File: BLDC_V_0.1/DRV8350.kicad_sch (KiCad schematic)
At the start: 12 parts, among them U1 DRV8350SRTVT

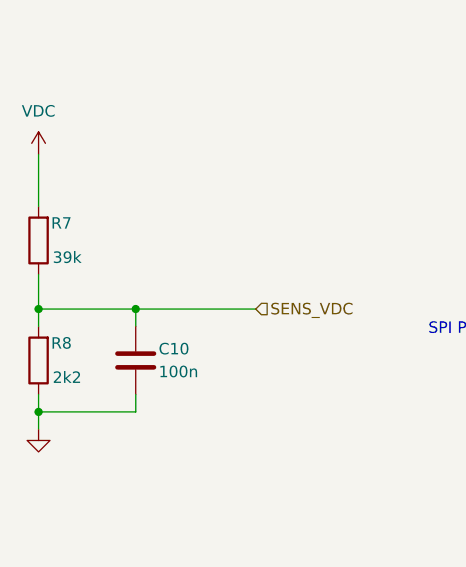
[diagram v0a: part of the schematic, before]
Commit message: Xtal changed 16MHz to 24MHz.
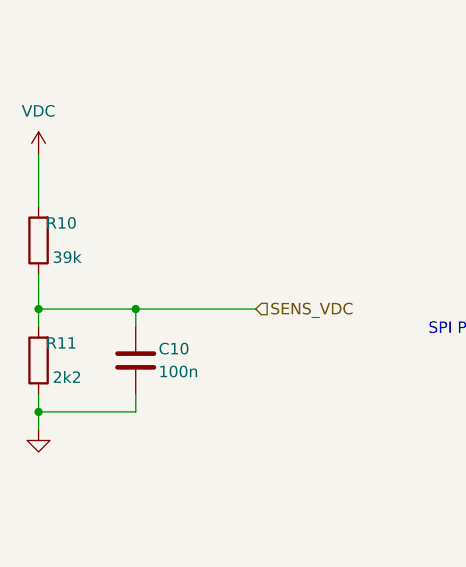
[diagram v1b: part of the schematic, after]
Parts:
- renumbered R7 to R10, R8 to R11
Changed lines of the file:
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@@
   (symbol (lib_id "Device:R") (at 28.575 80.645 180) (unit 1)
     (in_bom yes) (on_board yes) (dnp no)
-    (property "Reference" "R7" (at 31.115 78.74 0)
+    (property "Reference" "R10" (at 31.115 78.74 0)
       (effects (font (size 1.27 1.27)))
     )
@@
   (symbol (lib_id "Device:R") (at 28.575 93.98 180) (unit 1)
     (in_bom yes) (on_board yes) (dnp no)
-    (property "Reference" "R8" (at 31.115 92.075 0)
-      (effects (font (size 1.27 1.27)))
-    )
+    (property "Reference" "R11" (at 31.115 92.075 0)
+      (effects (font (size 1.27 1.27)))
+    )

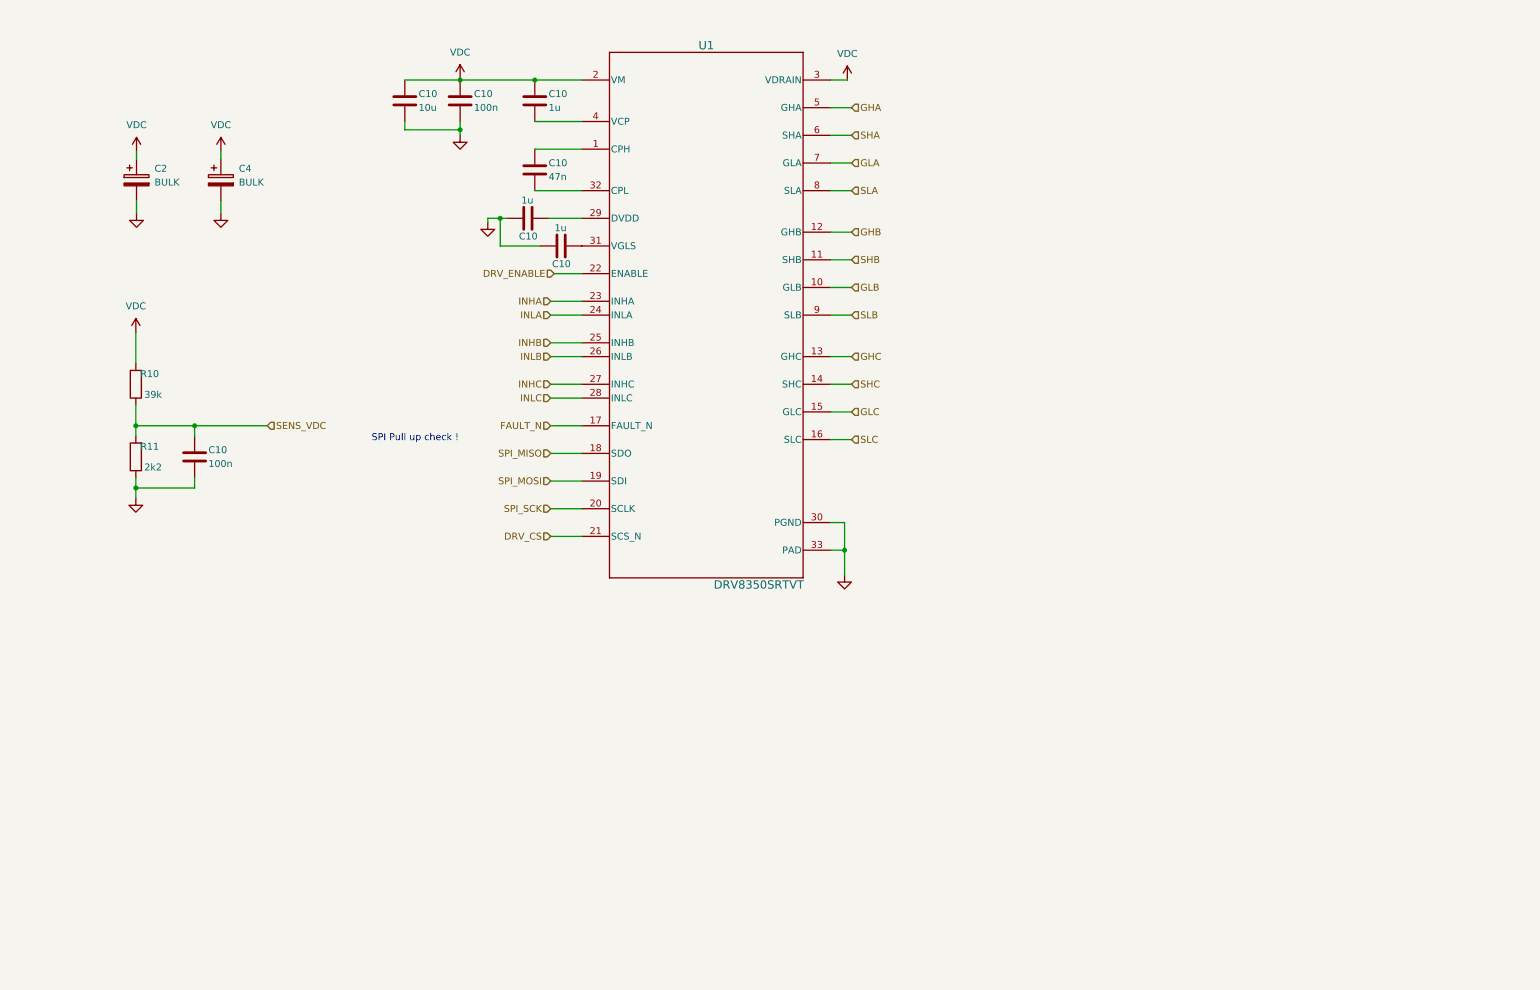
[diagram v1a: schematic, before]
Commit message: Connectors and CAN circuit added.
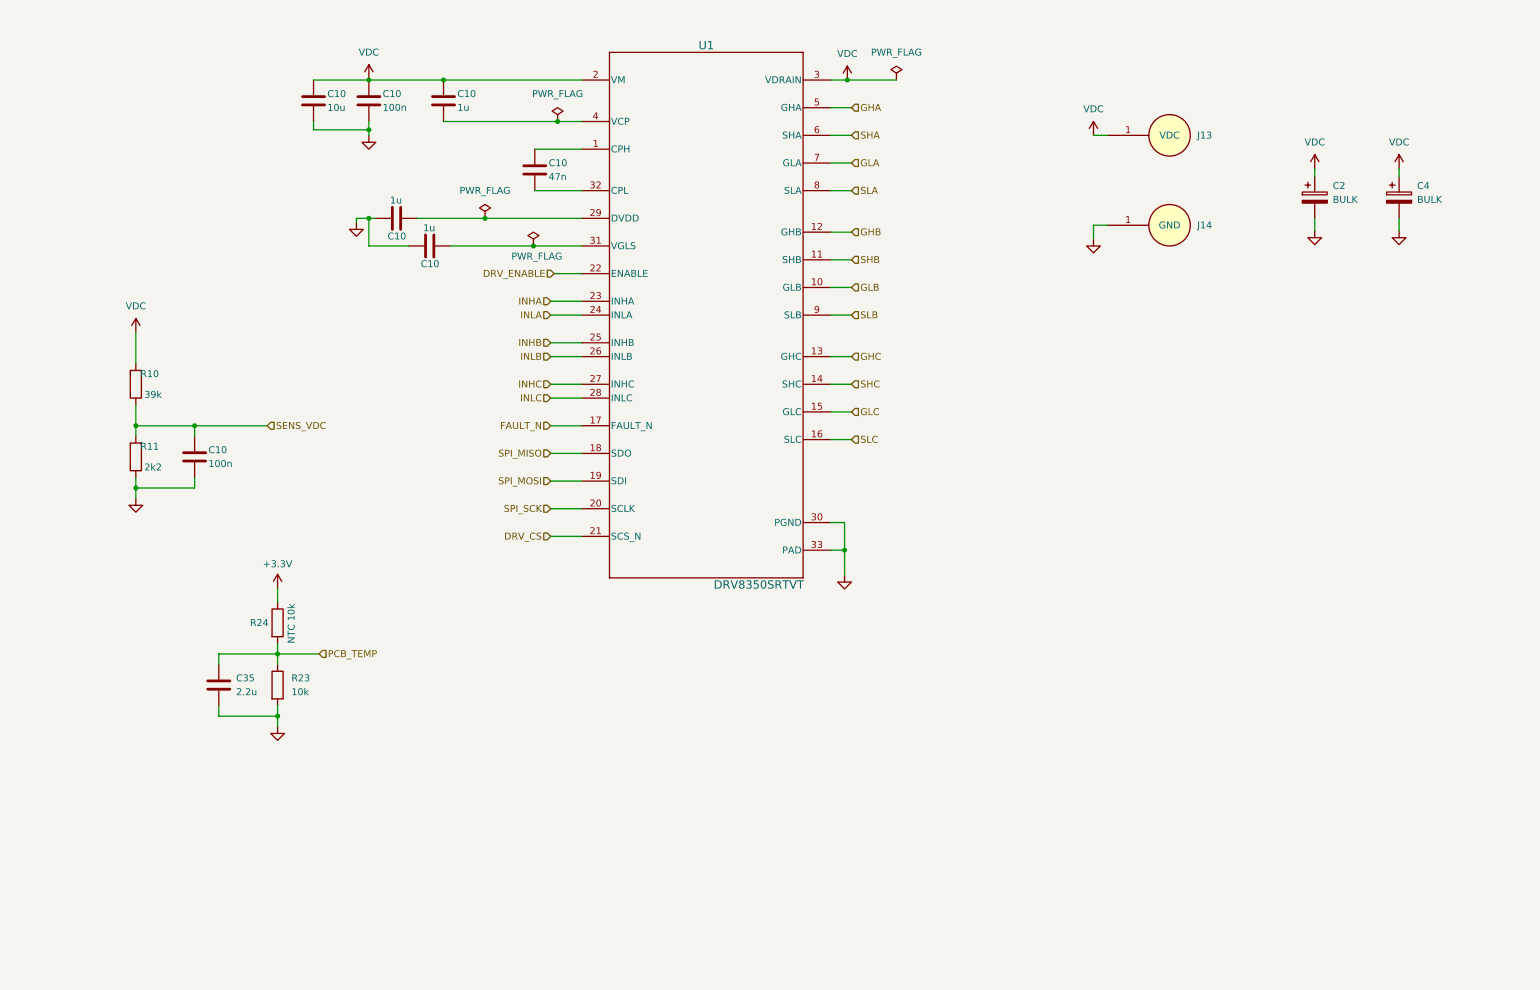
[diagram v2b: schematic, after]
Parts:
- added C35: 2.2u, symbol Device:C
- added J13: VDC, Connector:Power_Welding_Pad_10x10mm, symbol Connector_Generic:Power_Welding_PAD
- added J14: GND, Connector:Power_Welding_Pad_10x10mm, symbol Connector_Generic:Power_Welding_PAD
- added R23: 10k, symbol Device:R
- added R24: NTC 10k, symbol Device:R
- U1: footprint RTV0032E -> DRV-8350S:RTV0032E
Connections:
- net GND: now also C35.2, J14.1, R23.2
- net VDC: now also J13.1
- new net +3.3V: R24.1
- new net PCB_TEMP: C35.1, R23.1, R24.2
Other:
- note removed: "SPI Pull up check !"
- moved on the sheet: C10, C2, C4

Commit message: Schematic prototip done.
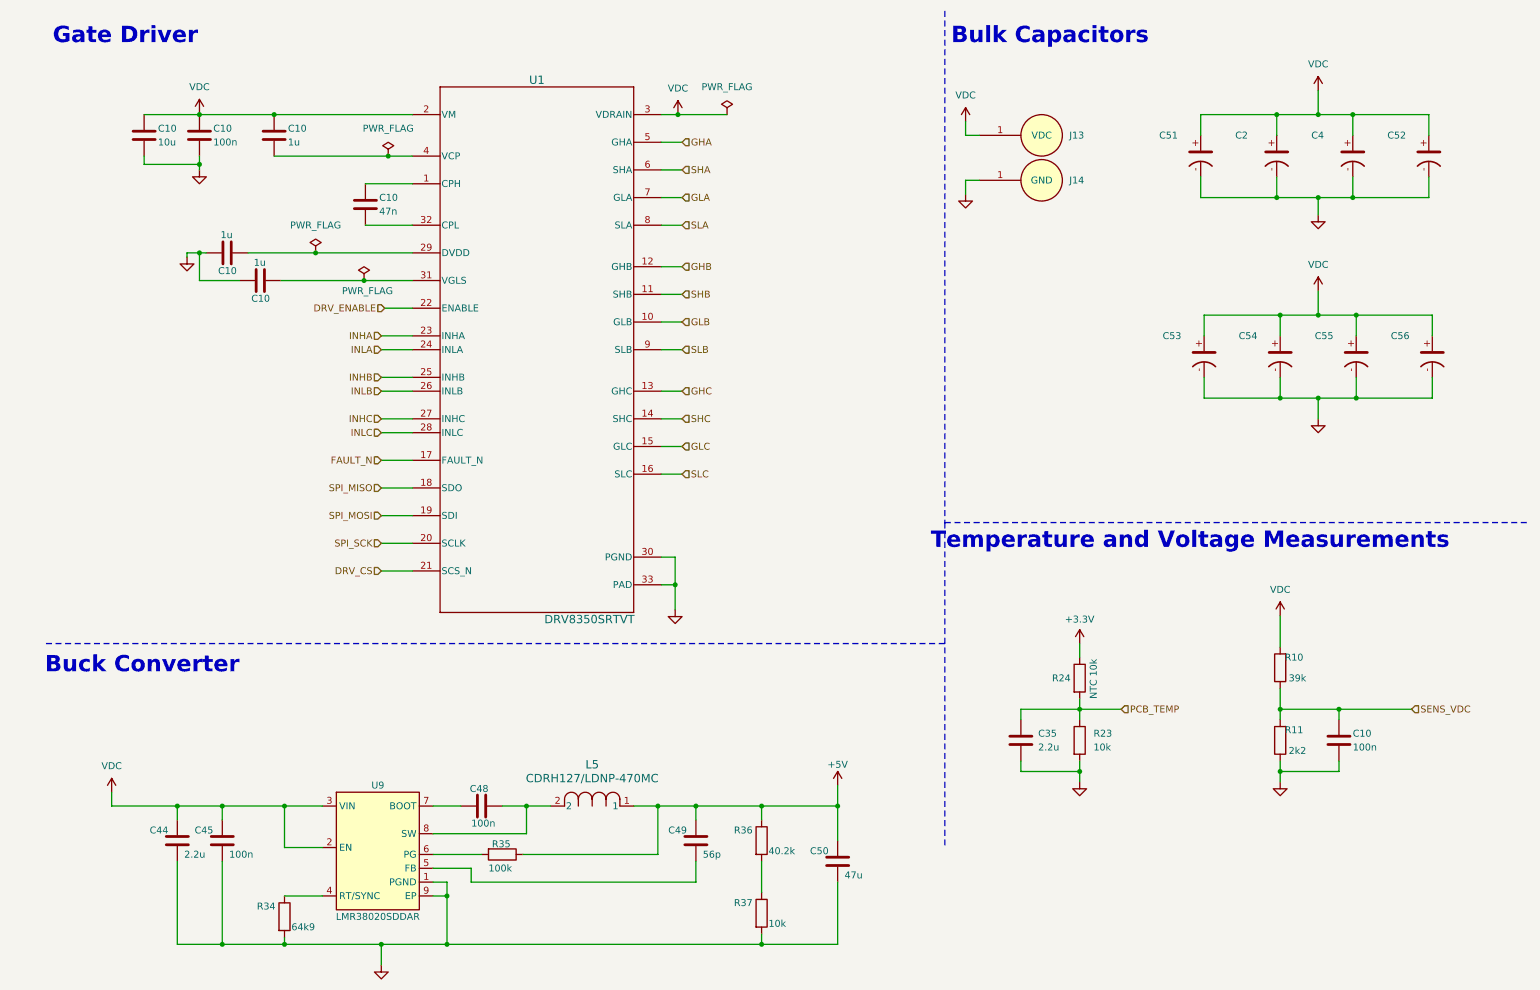
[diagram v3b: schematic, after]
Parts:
- removed C2, C4: BULK, symbol Device:C_Polarized
- added C2, C4, C51, C52, C53, C54, C55, C56: EEE-FN1J101V, EEHZT1E561UV, symbol BULK-Electrolitic-Cap:EEE-FN1J101V
- added C44: 2.2u, Capacitor_SMD:C_1210_3225Metric, symbol Device:C
- added C45: 100n, Capacitor_SMD:C_0805_2012Metric, symbol Device:C
- added C48: 100n, Capacitor_SMD:C_0402_1005Metric, symbol Device:C
- added C49: 56p, Capacitor_SMD:C_0201_0603Metric, symbol Device:C
- added C50: 47u, Capacitor_SMD:C_1210_3225Metric, symbol Device:C
- added L5: CDRH127/LDNP-470MC, CDRH127:IND_CDRH127&slash_LDNP-470MC_SUM, symbol CDRH127/LDNP-330MC:CDRH127_LDNP-470MC
- added R34: 64k9, Resistor_SMD:R_0603_1608Metric, symbol Device:R
- added R35: 100k, Resistor_SMD:R_0603_1608Metric, symbol Device:R
- added R36: 40.2k, Resistor_SMD:R_0402_1005Metric, symbol Device:R
- added R37: 10k, Resistor_SMD:R_0402_1005Metric, symbol Device:R
- added U9: LMR38020SDDAR, Converter_DCDC:LMR38020SDDAR, symbol Regulator_Switching:LMR38020DDAR
- C10: footprint (none) -> Capacitor_SMD:C_0402_1005Metric
- C10, C35: footprint (none) -> Capacitor_SMD:C_0603_1608Metric
- R10, R11, R23, R24: footprint (none) -> Resistor_SMD:R_0603_1608Metric
- U1: footprint DRV-8350S:RTV0032E -> RTV0032E
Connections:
- net GND: now also C2.-, C4.-, C44.2, C45.2, C50.2, C51.-, C52.-, C53.-, C54.-, C55.-, C56.-, R34.2, R37.2, U9.1 (PGND), U9.9 (EP)
- net VDC: now also C2.+, C4.+, C44.1, C45.1, C51.+, C52.+, C53.+, C54.+, C55.+, C56.+, U9.2 (EN), U9.3 (VIN)
- new net: R34.1, U9.4 (RT/SYNC)
- new net: R36.2, R37.1
- new net: C49.2, U9.5 (FB)
- new net: R35.2, U9.6 (PG)
- new net: C48.1, U9.7 (BOOT)
- new net: C48.2, L5.2, U9.8 (SW)
- new net +5V: C49.1, C50.1, L5.1, R35.1, R36.1
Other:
- note added: "Buck Converter"
- note added: "Bulk Capacitors"
- note added: "Gate Driver"
- note added: "Temperature and Voltage Measurements"
- moved on the sheet: C10, C35, J13, J14, R10, R11, R23, R24, U1

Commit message: PCB placement completed.
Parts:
- C2, C4, C52, C53, C54, C55, C56: footprint EEHZT1E561UV -> Capacitor:EEHZT1E561UV
- C51: footprint EEHZT1E561UV -> Capacitor:EEHZT1E561UV; Capacitans (none) -> 100u; Voltage Rating (none) -> 63V
- U1: footprint RTV0032E -> DRV-8350S:RTV0032E
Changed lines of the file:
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@@
       (effects (font (size 1.27 1.27)) (justify left) hide)
     )
-    (property "Footprint" "EEHZT1E561UV" (at 178.765 60.325 0)
+    (property "Footprint" "Capacitor:EEHZT1E561UV" (at 178.765 60.325 0)
       (effects (font (size 1.27 1.27)) (justify left top) hide)
     )
@@
       (effects (font (size 1.27 1.27)) (justify left) hide)
     )
-    (property "Footprint" "EEHZT1E561UV" (at 137.49 97.155 0)
+    (property "Footprint" "Capacitor:EEHZT1E561UV" (at 137.49 97.155 0)
       (effects (font (size 1.27 1.27)) (justify left top) hide)
     )
@@
       (effects (font (size 1.27 1.27)) (justify left) hide)
     )
-    (property "Footprint" "EEHZT1E561UV" (at 136.855 60.325 0)
+    (property "Footprint" "Capacitor:EEHZT1E561UV" (at 136.855 60.325 0)
       (effects (font (size 1.27 1.27)) (justify left top) hide)
     )
@@
     (property "Manufacturer_Part_Number" "EEE-FN1J101V" (at -563.145 60.325 0)
       (effects (font (size 1.27 1.27)) (justify left top) hide)
+    )
+    (property "Capacitans" "100u" (at 219.075 40.005 90)
+      (effects (font (size 1.27 1.27)))
+    )
+    (property "Voltage Rating" "63V" (at 224.155 38.735 90)
+      (effects (font (size 1.27 1.27)) hide)
     )
     (pin "+")
@@
       (effects (font (size 1.524 1.524)))
     )
-    (property "Footprint" "RTV0032E" (at 102.235 74.295 0)
+    (property "Footprint" "DRV-8350S:RTV0032E" (at 102.235 74.295 0)
       (effects (font (size 1.27 1.27) italic) hide)
     )
@@
       (effects (font (size 1.27 1.27)) (justify left) hide)
     )
-    (property "Footprint" "EEHZT1E561UV" (at 165.43 97.155 0)
+    (property "Footprint" "Capacitor:EEHZT1E561UV" (at 165.43 97.155 0)
       (effects (font (size 1.27 1.27)) (justify left top) hide)
     )
@@
       (effects (font (size 1.27 1.27)) (justify left) hide)
     )
-    (property "Footprint" "EEHZT1E561UV" (at 179.4 97.155 0)
+    (property "Footprint" "Capacitor:EEHZT1E561UV" (at 179.4 97.155 0)
       (effects (font (size 1.27 1.27)) (justify left top) hide)
     )
@@
       (effects (font (size 1.27 1.27)) (justify left) hide)
     )
-    (property "Footprint" "EEHZT1E561UV" (at 164.795 60.325 0)
+    (property "Footprint" "Capacitor:EEHZT1E561UV" (at 164.795 60.325 0)
       (effects (font (size 1.27 1.27)) (justify left top) hide)
     )
@@
       (effects (font (size 1.27 1.27)) (justify left) hide)
     )
-    (property "Footprint" "EEHZT1E561UV" (at 151.46 97.155 0)
+    (property "Footprint" "Capacitor:EEHZT1E561UV" (at 151.46 97.155 0)
       (effects (font (size 1.27 1.27)) (justify left top) hide)
     )
@@
       (effects (font (size 1.27 1.27)) (justify left) hide)
     )
-    (property "Footprint" "EEHZT1E561UV" (at 150.825 60.325 0)
-      (effects (font (size 1.27 1.27)) (justify left top) hide)
-    )
+    (property "Footprint" "Capacitor:EEHZT1E561UV" (at 150.825 60.325 0)
+      (effects (font (size 1.27 1.27)) (justify left top) hide)
+    )
